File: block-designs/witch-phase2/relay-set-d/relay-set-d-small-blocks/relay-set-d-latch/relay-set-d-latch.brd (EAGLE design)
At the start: 99.1 x 50.8 mm, 53 parts, among them IC1 74LVC1G125DBV, IC10 741G175, IC11 74LVC1G06DBV, IC12 74LVC1G06DBV, IC13 74LVC1G06DBV, IC14 74LVC1G06DBV, IC15 74LVC1G06DBV, IC2 74LVC1G125DBV, IC3 74LVC1G125DBV, IC4 74LVC1G125DBV, IC5 74LVC1G125DBV, IC6 741G175, IC7 741G175, IC8 741G175, IC9 741G175, Q1 MMBT2907ALT1SMD, Q2 MMBT2907ALT1SMD

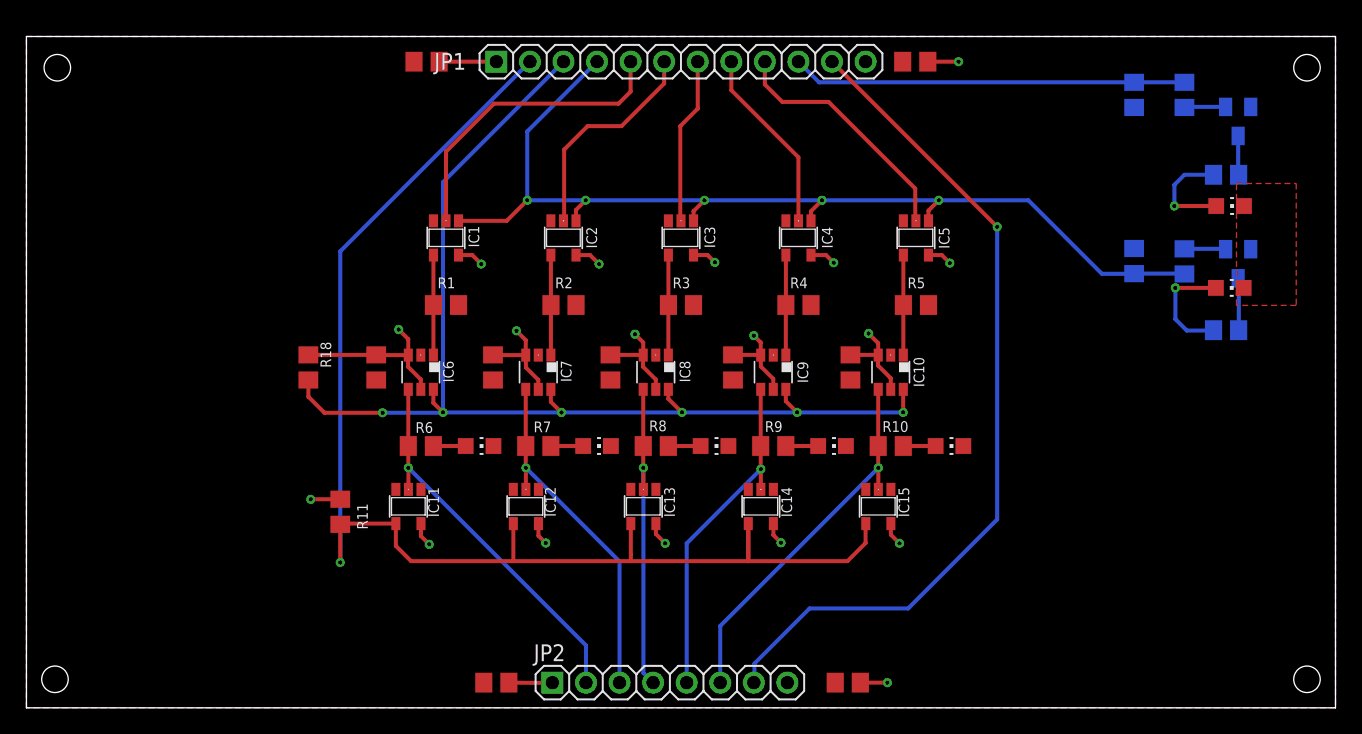
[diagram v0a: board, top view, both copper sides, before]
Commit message: adjust borders for ground/vcc plains and size to match 1.1inch grids
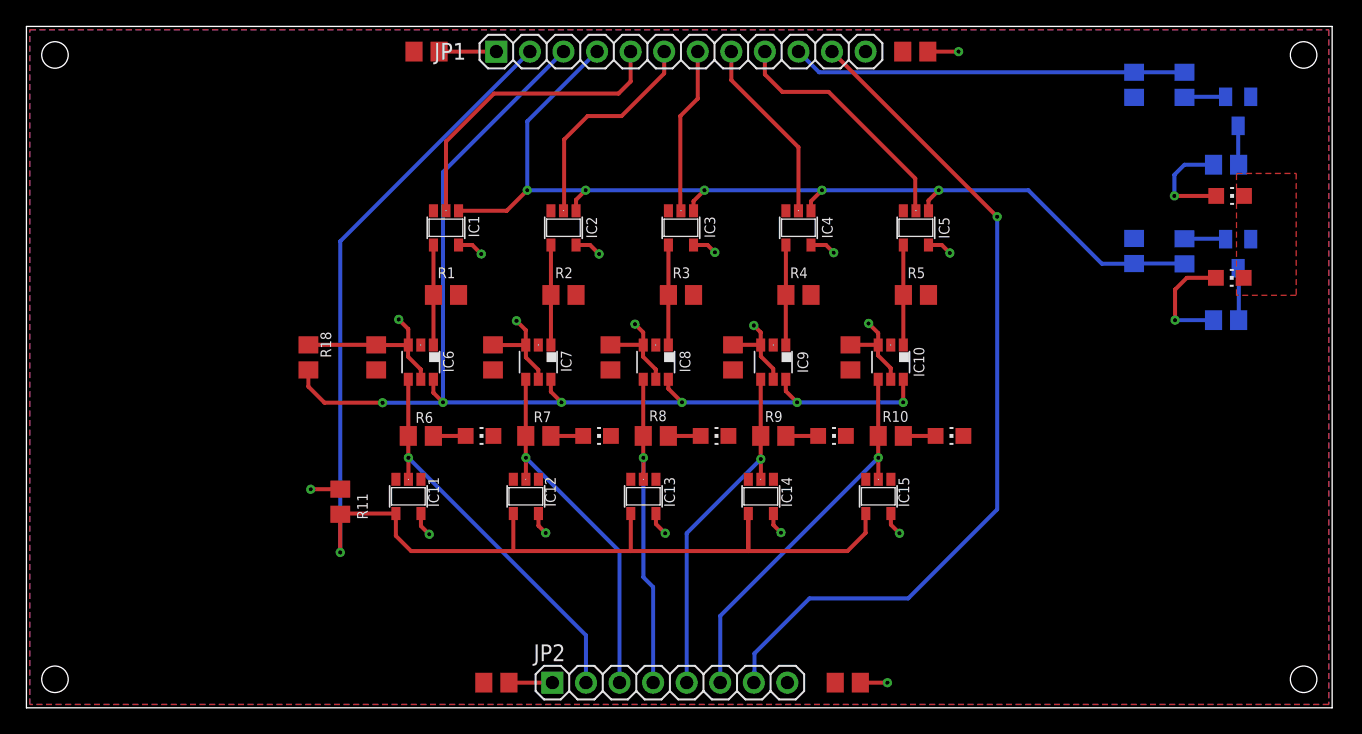
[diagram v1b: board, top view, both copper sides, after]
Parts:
- moved C5 0.76 mm to (35.3, 26.5)
- moved C6 0.76 mm to (44.2, 26.5)
- moved C7 0.76 mm to (53.5, 26.5)
- moved C8 0.76 mm to (62.4, 26.5)
- moved C9 0.76 mm to (26.5, 26.5)
- moved IC1 0.76 mm to (31.8, 36.3)
- moved IC10 0.76 mm to (65.4, 26.2)
- moved IC2 0.76 mm to (40.6, 36.3)
- moved IC3 0.76 mm to (49.5, 36.3)
- moved IC4 0.76 mm to (58.4, 36.3)
- moved IC5 0.76 mm to (67.3, 36.3)
- moved IC6 0.76 mm to (29.8, 26.2)
- moved IC7 0.76 mm to (38.7, 26.2)
- moved IC8 0.76 mm to (47.6, 26.2)
- moved IC9 0.76 mm to (56.5, 26.2)
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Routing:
- net DD_OUT: track 26.1 -> 26.8 mm
- net DE_OUT: track 28.8 -> 29.6 mm
- net DC_OUT: track 24.1 -> 24.9 mm
- net DB_OUT: track 26.8 -> 27.5 mm
- net DA_OUT: track 29.4 -> 30.2 mm
- net DSA-DSB: track 64.2 -> 64.9 mm
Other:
- board size 99.1 x 50.8 mm -> 98.8 x 51.6 mm

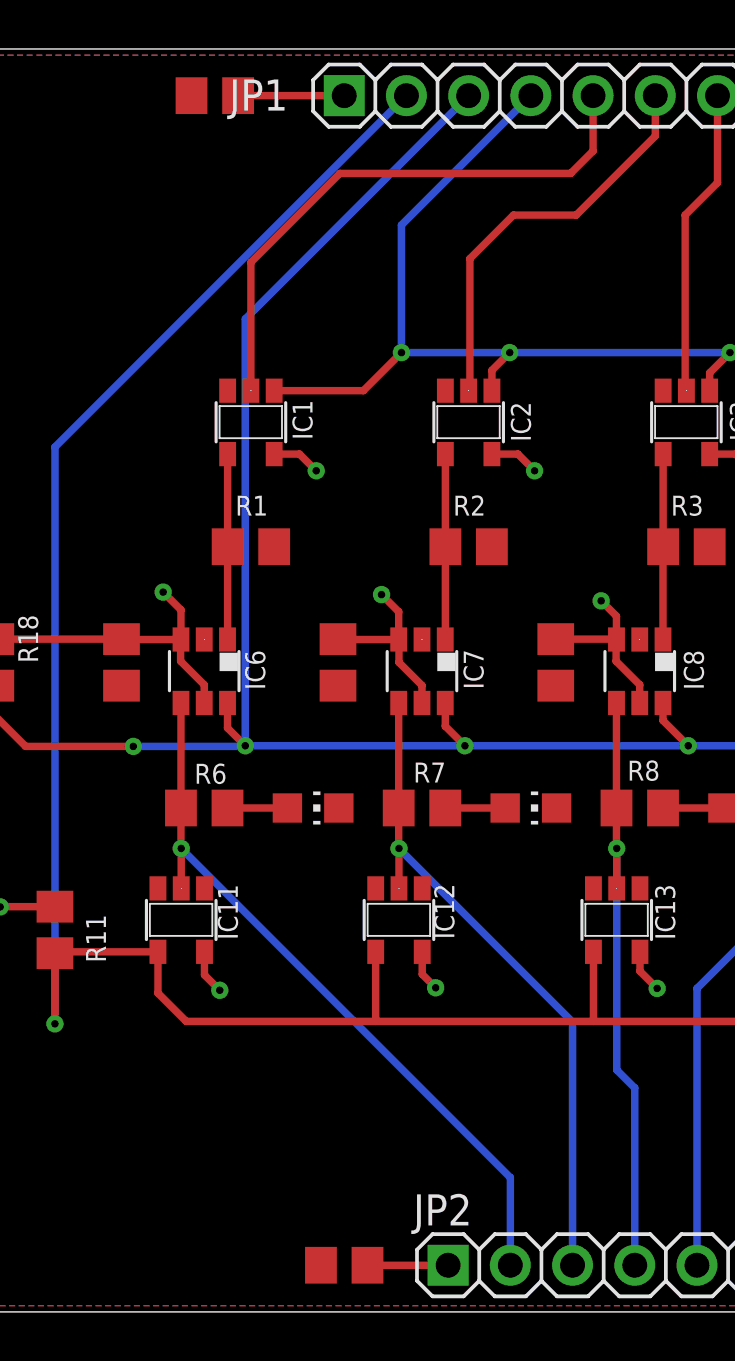
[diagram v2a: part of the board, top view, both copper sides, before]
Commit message: updated designs for new labeling and spacing
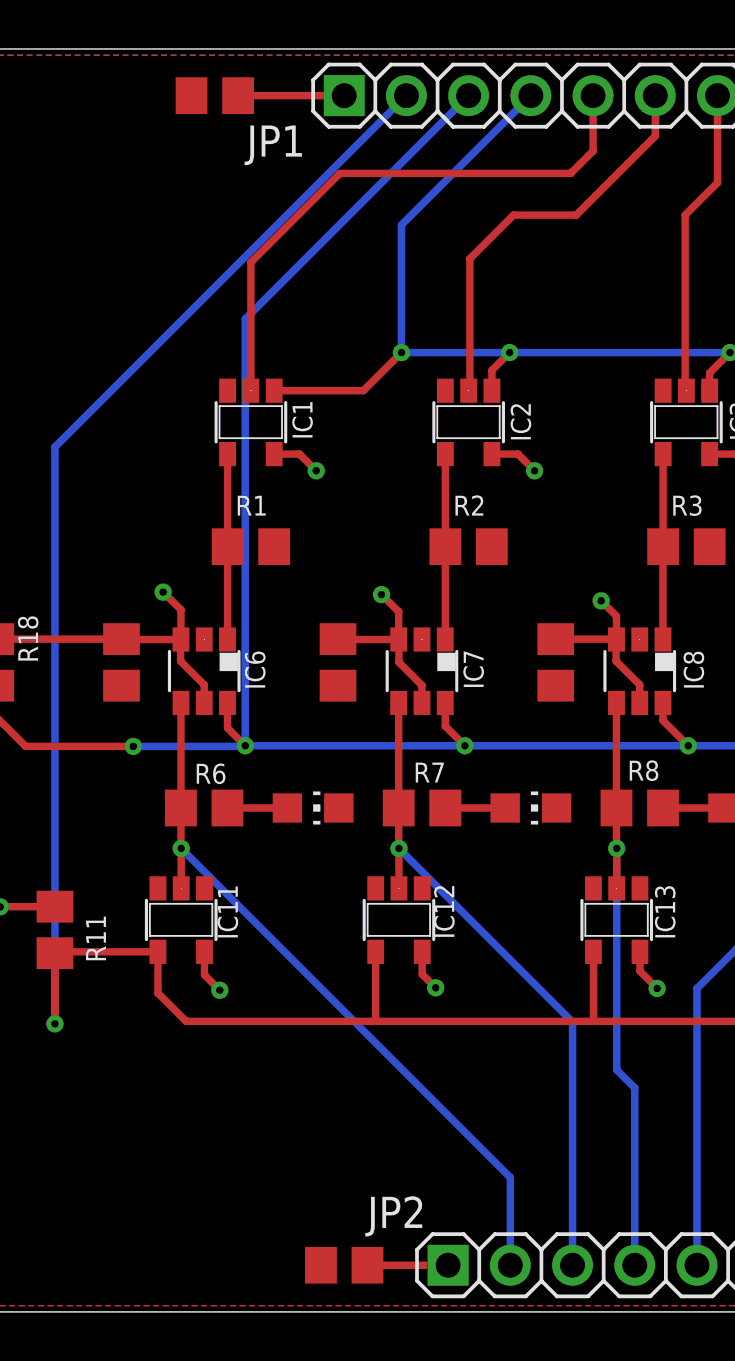
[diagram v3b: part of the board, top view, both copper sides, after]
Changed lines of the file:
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@@
 <elements>
 <element name="JP2" library="pinhead" package="1X08" value="" x="48.6918" y="1.905" smashed="yes">
-<attribute name="NAME" x="38.3794" y="3.5306" size="1.27" layer="25" ratio="10"/>
+<attribute name="NAME" x="36.4998" y="3.429" size="1.27" layer="25" ratio="10"/>
 <attribute name="VALUE" x="33.4518" y="-1.27" size="1.27" layer="27"/>
 </element>
@@
 </element>
 <element name="JP1" library="pinhead" package="1X12" value="" x="49.53" y="49.657" smashed="yes">
-<attribute name="NAME" x="30.861" y="49.0474" size="1.27" layer="25" ratio="10"/>
+<attribute name="NAME" x="31.5722" y="47.1678" size="1.27" layer="25" ratio="10"/>
 <attribute name="VALUE" x="34.29" y="46.482" size="1.27" layer="27"/>
 </element>

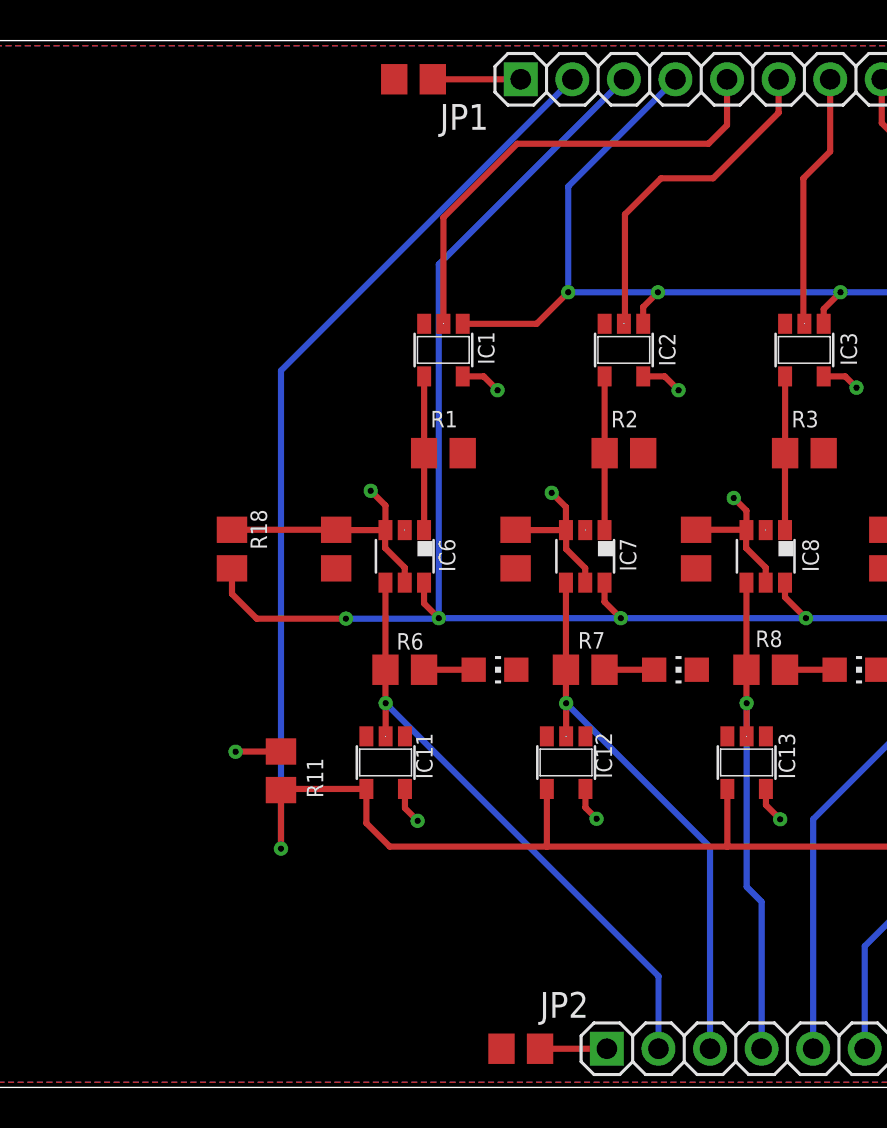
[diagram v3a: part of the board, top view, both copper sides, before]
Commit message: add inverting schmitt trigger to valid data detect output
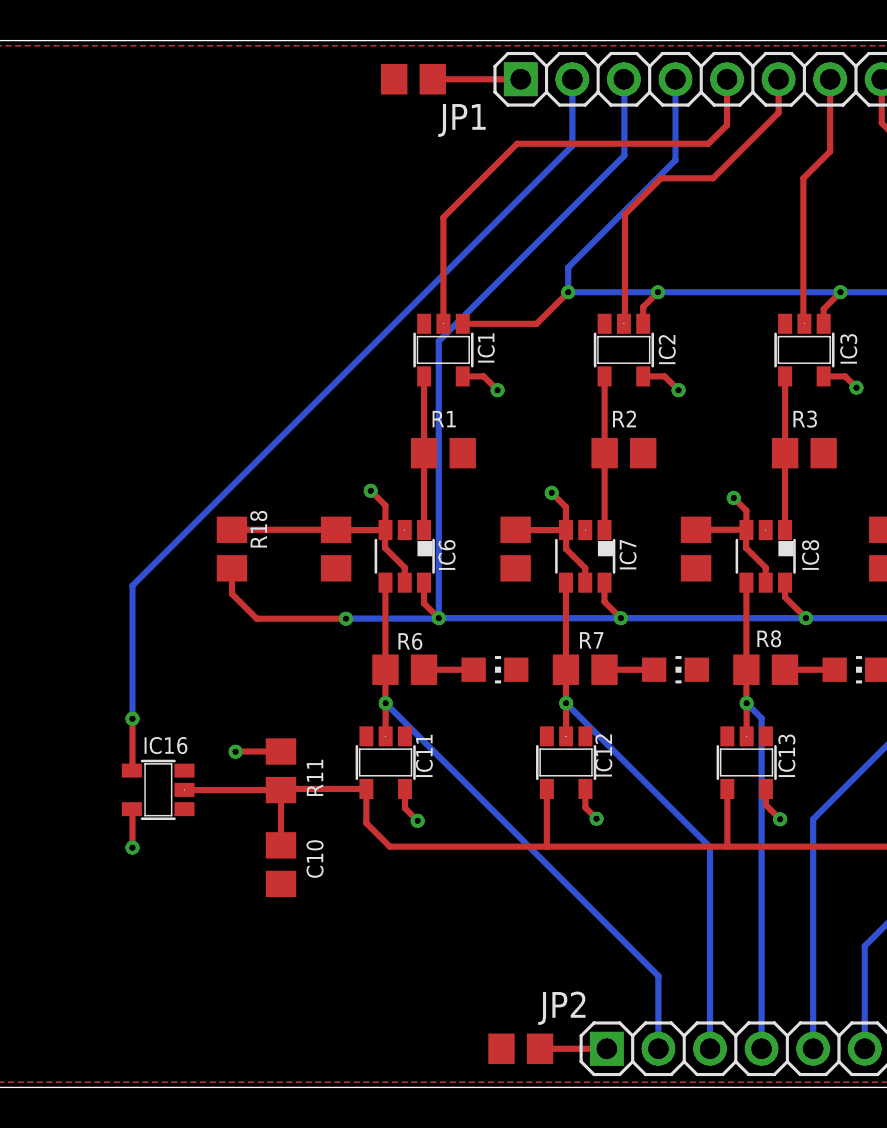
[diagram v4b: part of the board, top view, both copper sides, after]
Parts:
- added C10: 1uF, resistor:C0805
- added IC16: 74LVC1G14DBV, 74xx-little-us:SOT23-5
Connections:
- new net VALDATA: IC16.4, JP1.2
- net DATA_N: now also C10.1, IC16.2; no longer JP1.2
- net GND: now also C10.2, IC16.3
- net VCC: now also IC16.5
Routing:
- net VALDATA: track 0.00 -> 43.1 mm, vias 0 -> 1
- net DATA_N: track 102.1 -> 62.9 mm, vias 1 -> 0
- net VCC: track 74.2 -> 76.1 mm, vias 18 -> 19
